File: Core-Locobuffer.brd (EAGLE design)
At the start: 33 x 47 mm, 17 parts, among them J1 RJ12, Q1 2N2222, U1 LM393M

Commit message: added values for connectors
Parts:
- COMS, I2C: value (none) -> 0.100
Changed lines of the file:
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@@
 </element>
 <element name="U$1" library="SPCoast" package="ARDUINO-PRO-MICRO-NOSILK" value="ARDUINO-PRO-MICRO" x="16.51" y="15.24" rot="R180"/>
-<element name="I2C" library="SPCoast" package="1X04_LOCK" value="" x="29.591" y="22.479" smashed="yes" rot="R270">
+<element name="I2C" library="SPCoast" package="1X04_LOCK" value="0.100" x="29.591" y="22.479" smashed="yes" rot="R270">
 <attribute name="NAME" x="33.3248" y="20.6502" size="1.27" layer="25" ratio="10" rot="R270"/>
 <attribute name="VALUE" x="26.416" y="23.749" size="1.27" layer="27" rot="R270"/>
 </element>
-<element name="COMS" library="SPCoast" package="1X04_LOCK" value="" x="29.464" y="10.16" smashed="yes" rot="R270">
+<element name="COMS" library="SPCoast" package="1X04_LOCK" value="0.100" x="29.464" y="10.16" smashed="yes" rot="R270">
 <attribute name="NAME" x="33.1978" y="8.9662" size="1.27" layer="25" ratio="10" rot="R270"/>
 <attribute name="VALUE" x="26.289" y="11.43" size="1.27" layer="27" rot="R270"/>

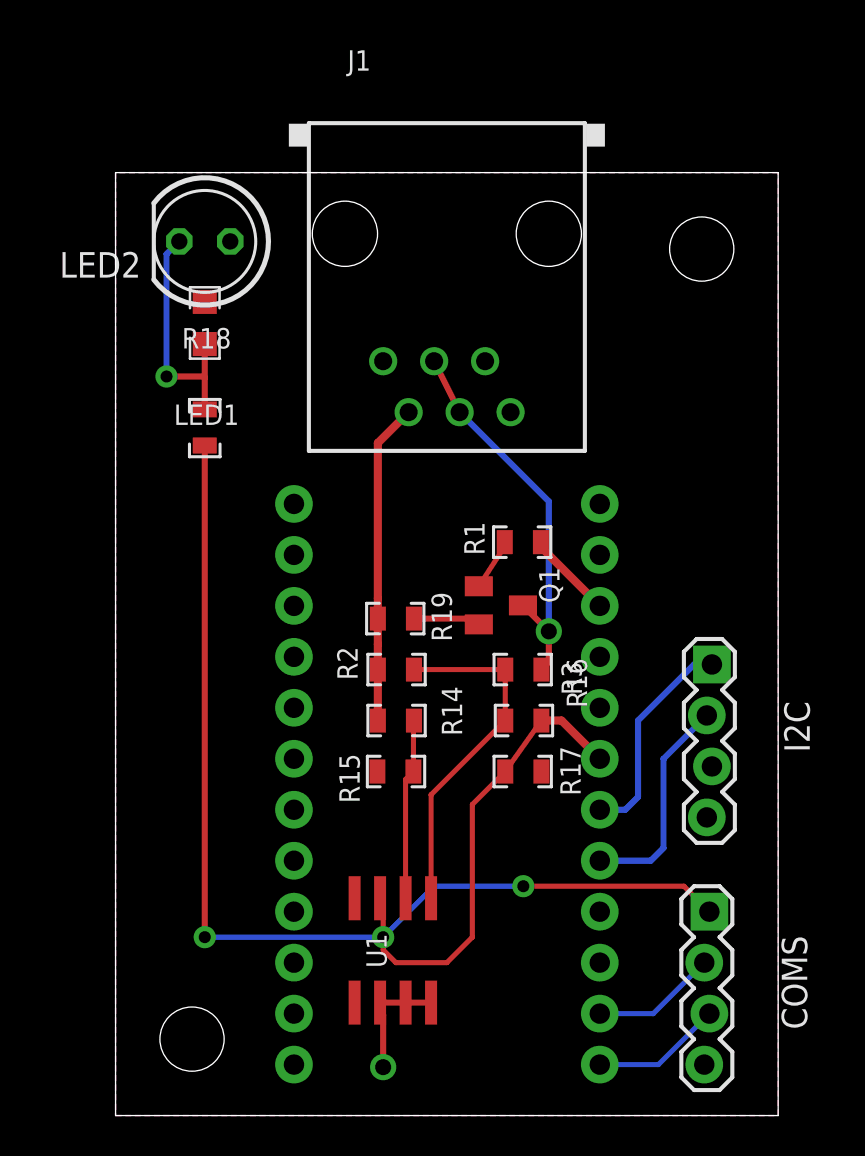
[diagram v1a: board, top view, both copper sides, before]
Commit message: normalized values
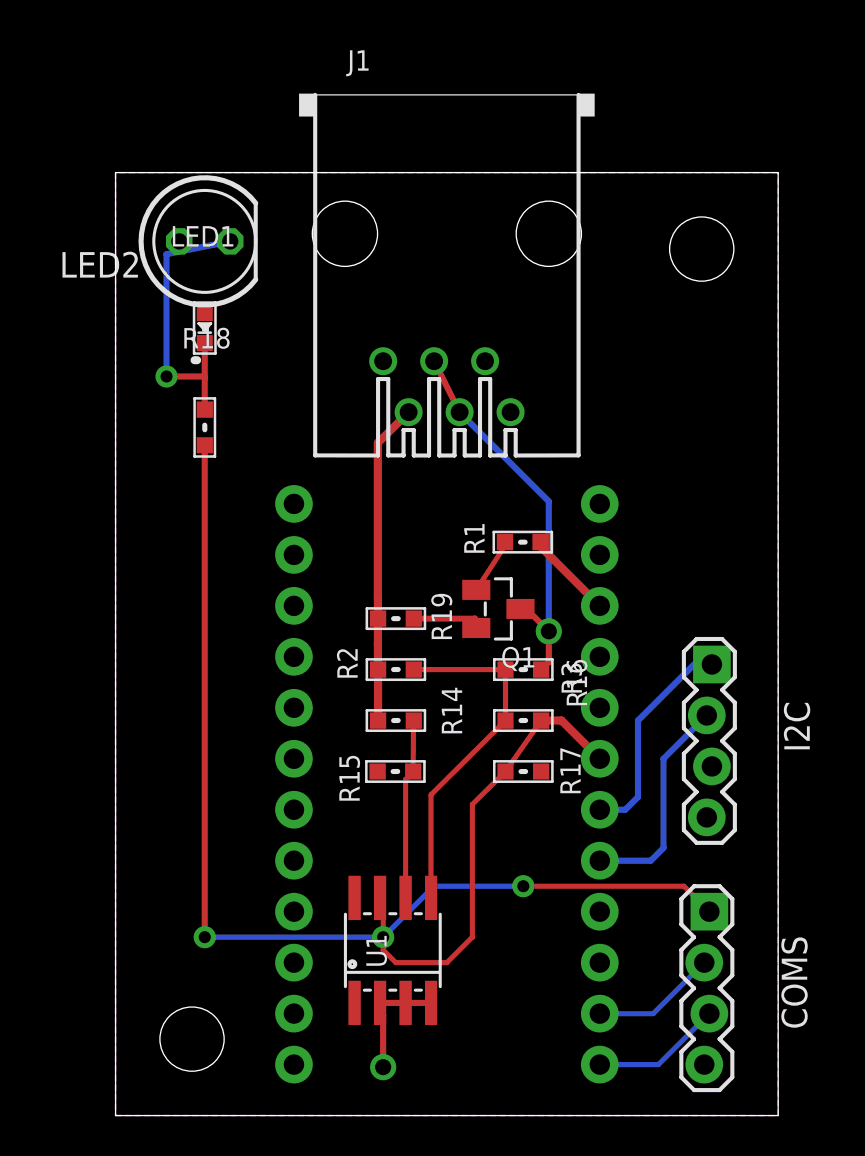
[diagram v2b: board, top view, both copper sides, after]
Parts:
- J1: value RJ12 -> RJ12/6; device SPCoast:RJ25 -> SPCoast:RJ25-PANEL
- LED1: device SPCoast:0805-LED -> SPCoast:0603-LED
- LED2: value Blue -> B
- R1, R14, R15, R16, R17, R18, R19, R2, R3: device SPCoast:0805-RES -> SPCoast:0603-RES
- U$1: value ARDUINO-PRO-MICRO -> PRO-MICRO
- moved LED1 0.25 mm to (4.45, 39.2), turned to 90 degrees
- moved Q1 0.22 mm to (19.1, 25.2), turned to 180 degrees
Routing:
- net N$2: track 12.2 -> 14.6 mm
